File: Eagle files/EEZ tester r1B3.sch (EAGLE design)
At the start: 89 parts, among them IC2 LM5574MTX/NOPB, K1 RT314005, Q1 2N7002, Q2 2N7002, Q3 2N7002, Q4 2N7002, Q5 2N7002, Q6 2N7002, SW1 1301.9316, SW2 1301.9316, X1 39303035, X3 SSW-113-02-S-D-RA, X4 ???, X6 09185166324

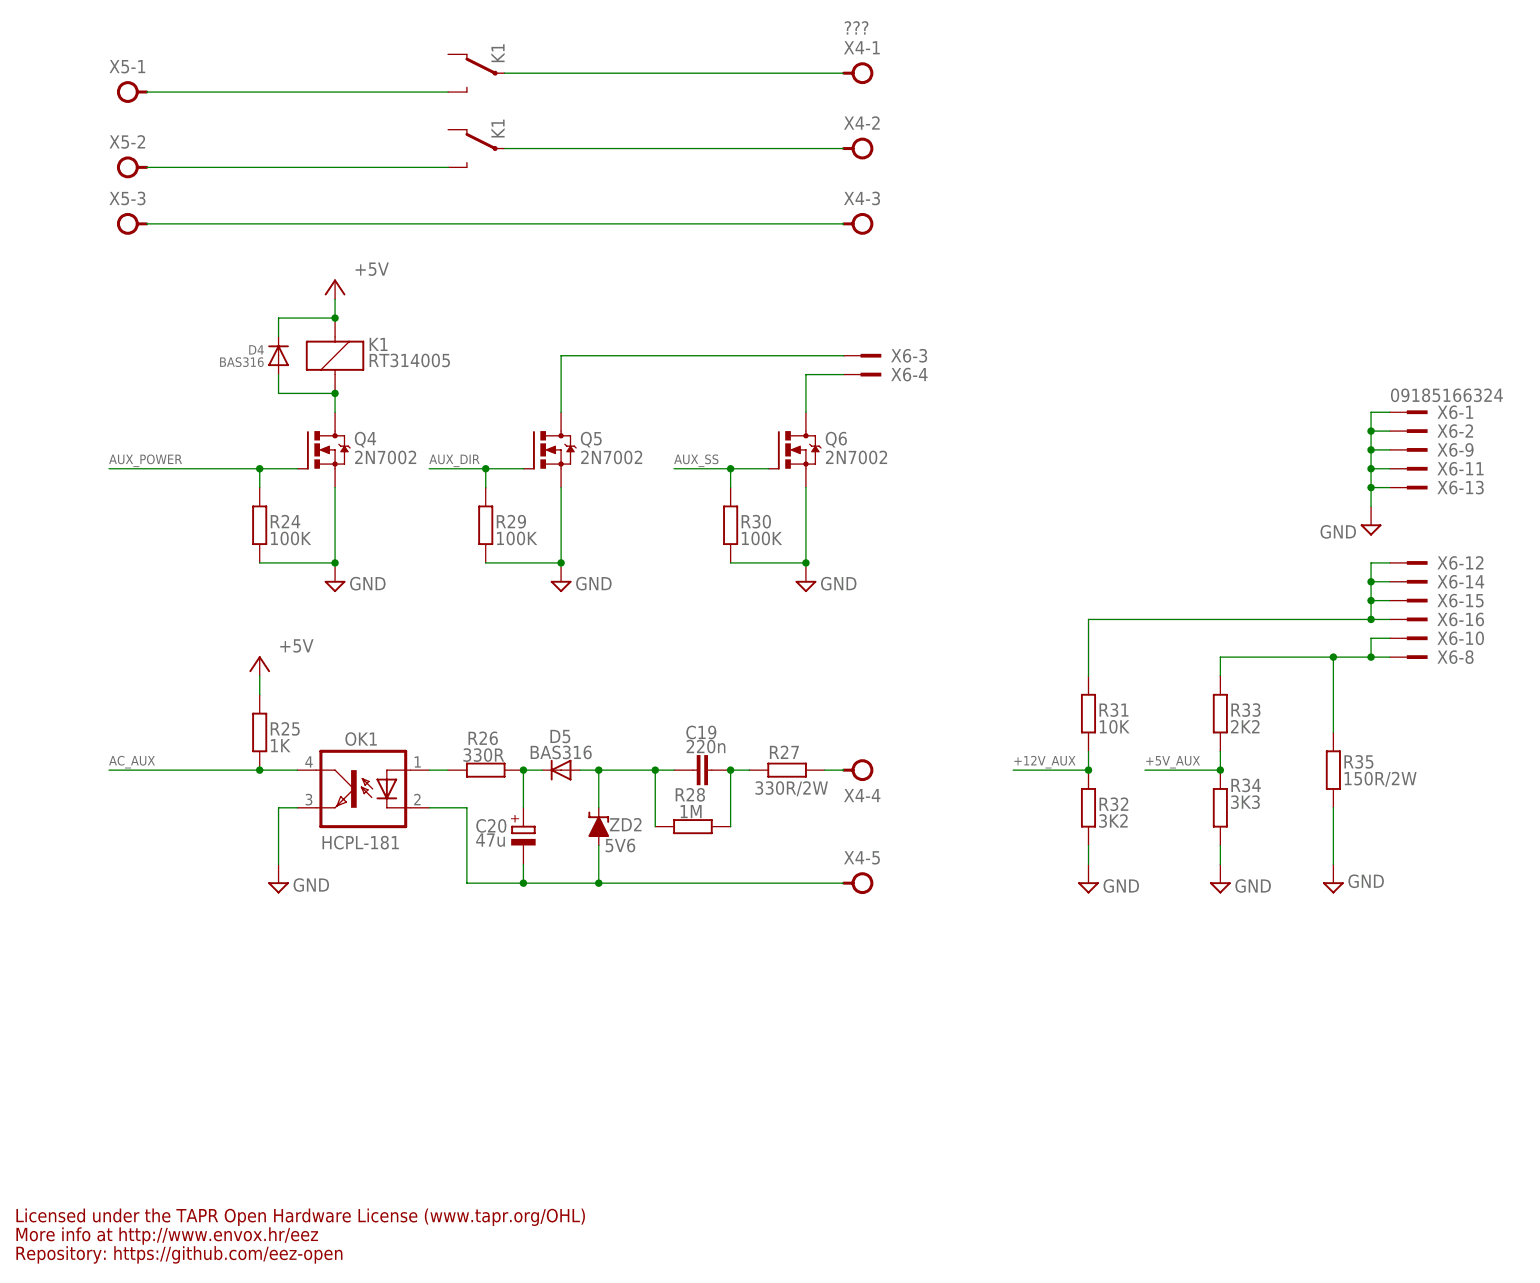
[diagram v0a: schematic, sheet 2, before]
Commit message: Arduino rotated ICSP fixed
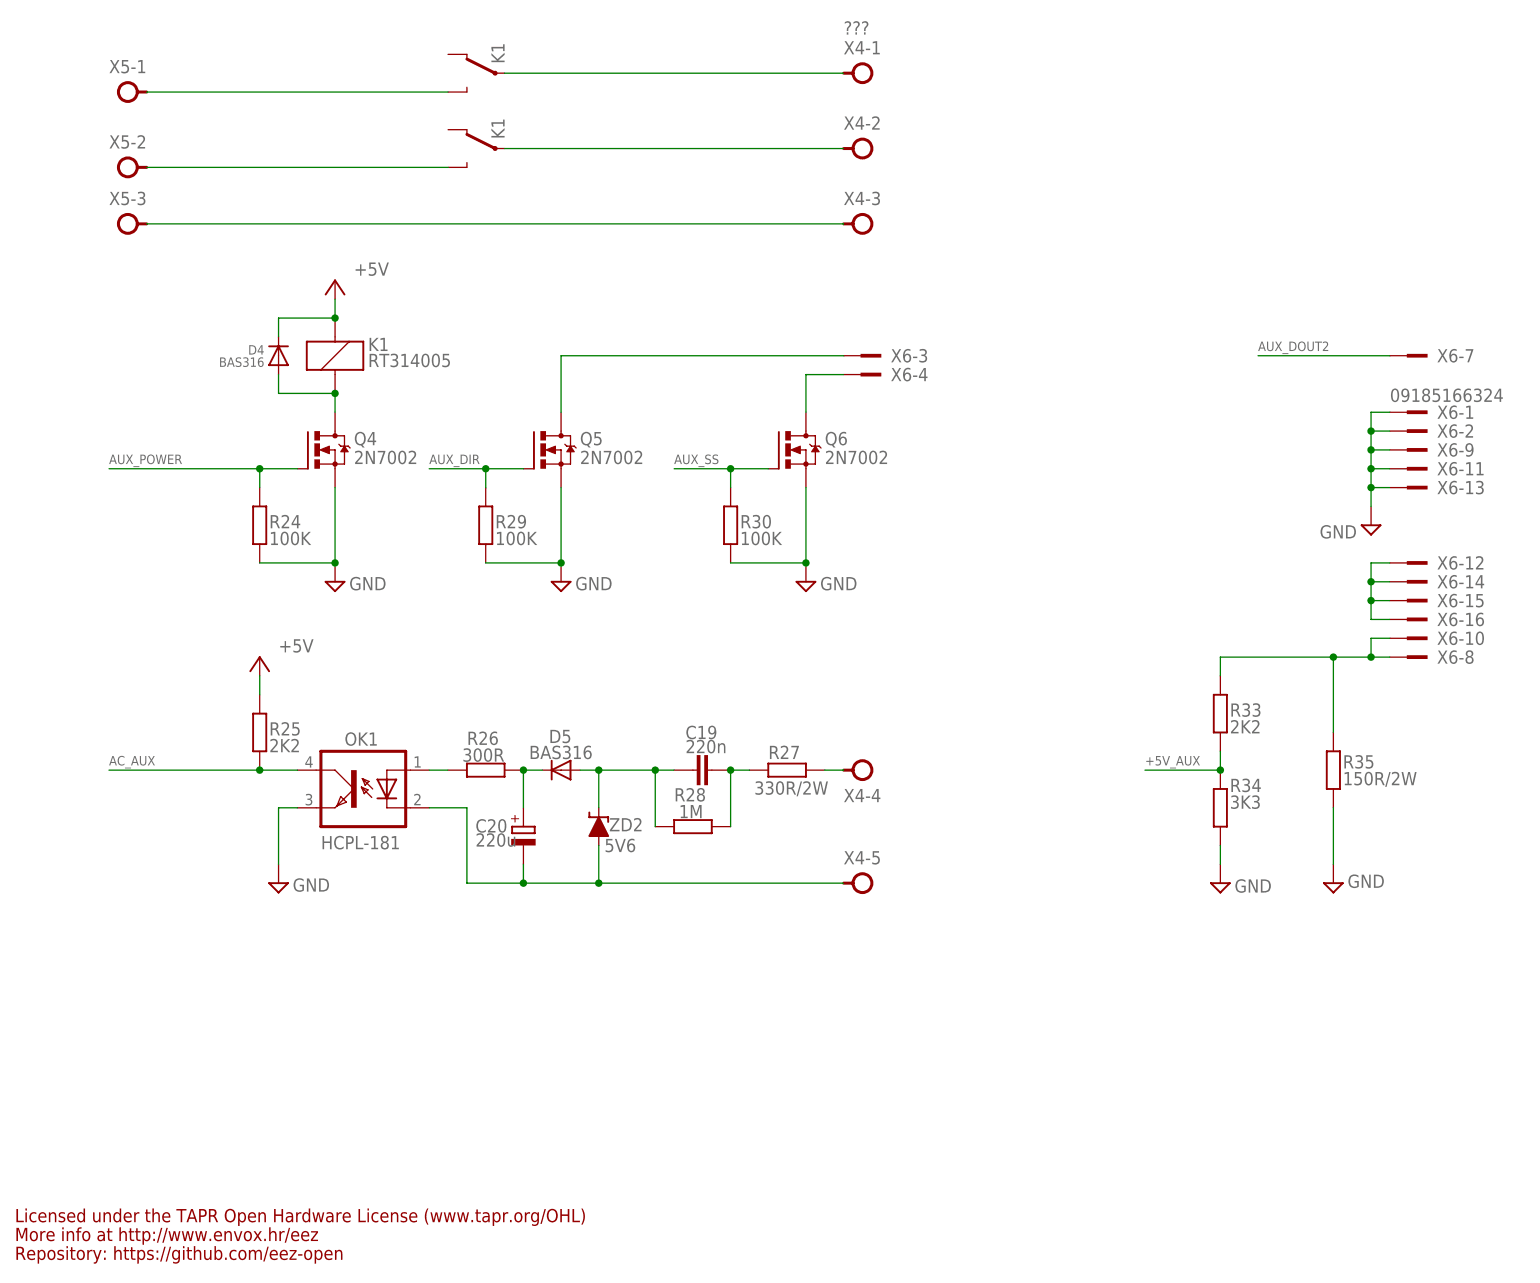
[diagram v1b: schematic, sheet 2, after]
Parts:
- removed R31: 10K, rcl:R-EU_R0805
- removed R32: 3K2, rcl:R-EU_R0805
- C17: value 4n7 -> 6n8
- C20: value 47u -> 220u
- L2: value 100uH -> 220uH
- R17: value (none) -> 10K
- R18: value (none) -> 20K
- R21: value 30K -> 18K
- R22: value 11K -> 20K
- R25: value 1K -> 2K2
- R26: value 330R -> 300R
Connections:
- net N$12 renamed LED_GREEN
- net N$14 renamed LED_RED
- net N$17 renamed SW2
- net N$18 renamed DC_ENABLE
- net N$6 renamed RPROG
- net N$8 renamed LOAD_ENABLE
- removed net +12V_AUX: MCU-ANALOG.ADC0, R31.1, R32.2
- new net AUX_DOUT2: MCU-ANALOG.ADC0, X6-7.1
- net GND: no longer R32.1
- net N$38: no longer R31.2
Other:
- note added: "Dout2 (Output) 7"
- note removed: "Sync (Output) 7"

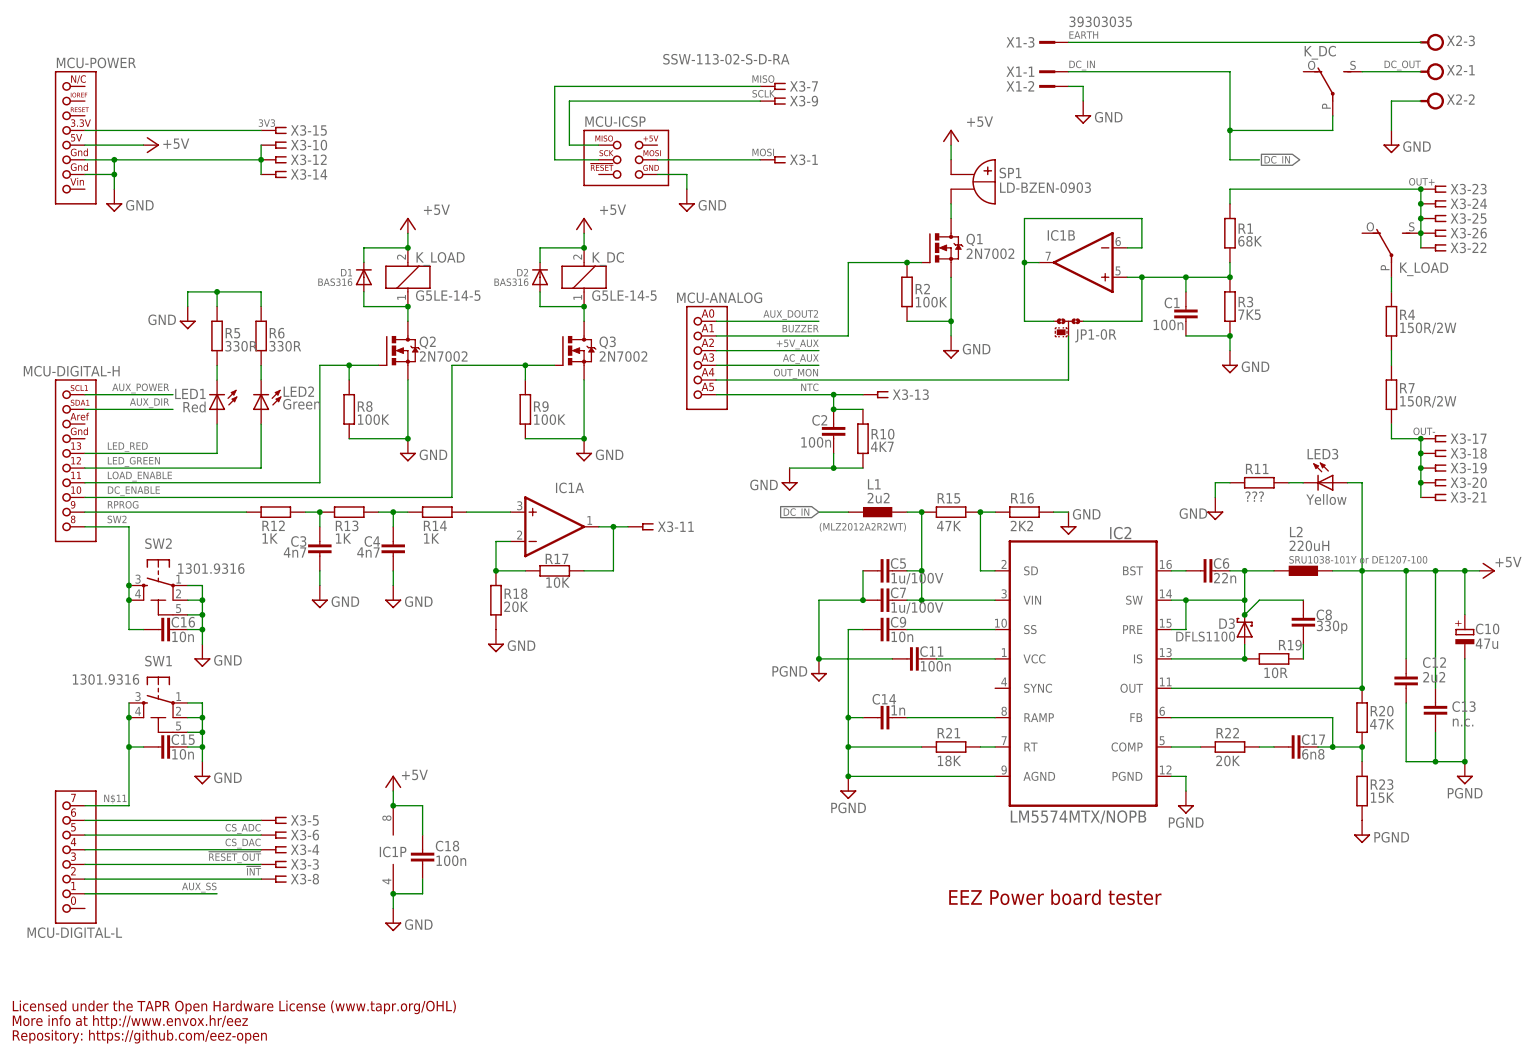
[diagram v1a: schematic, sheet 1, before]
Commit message: parts value corrections
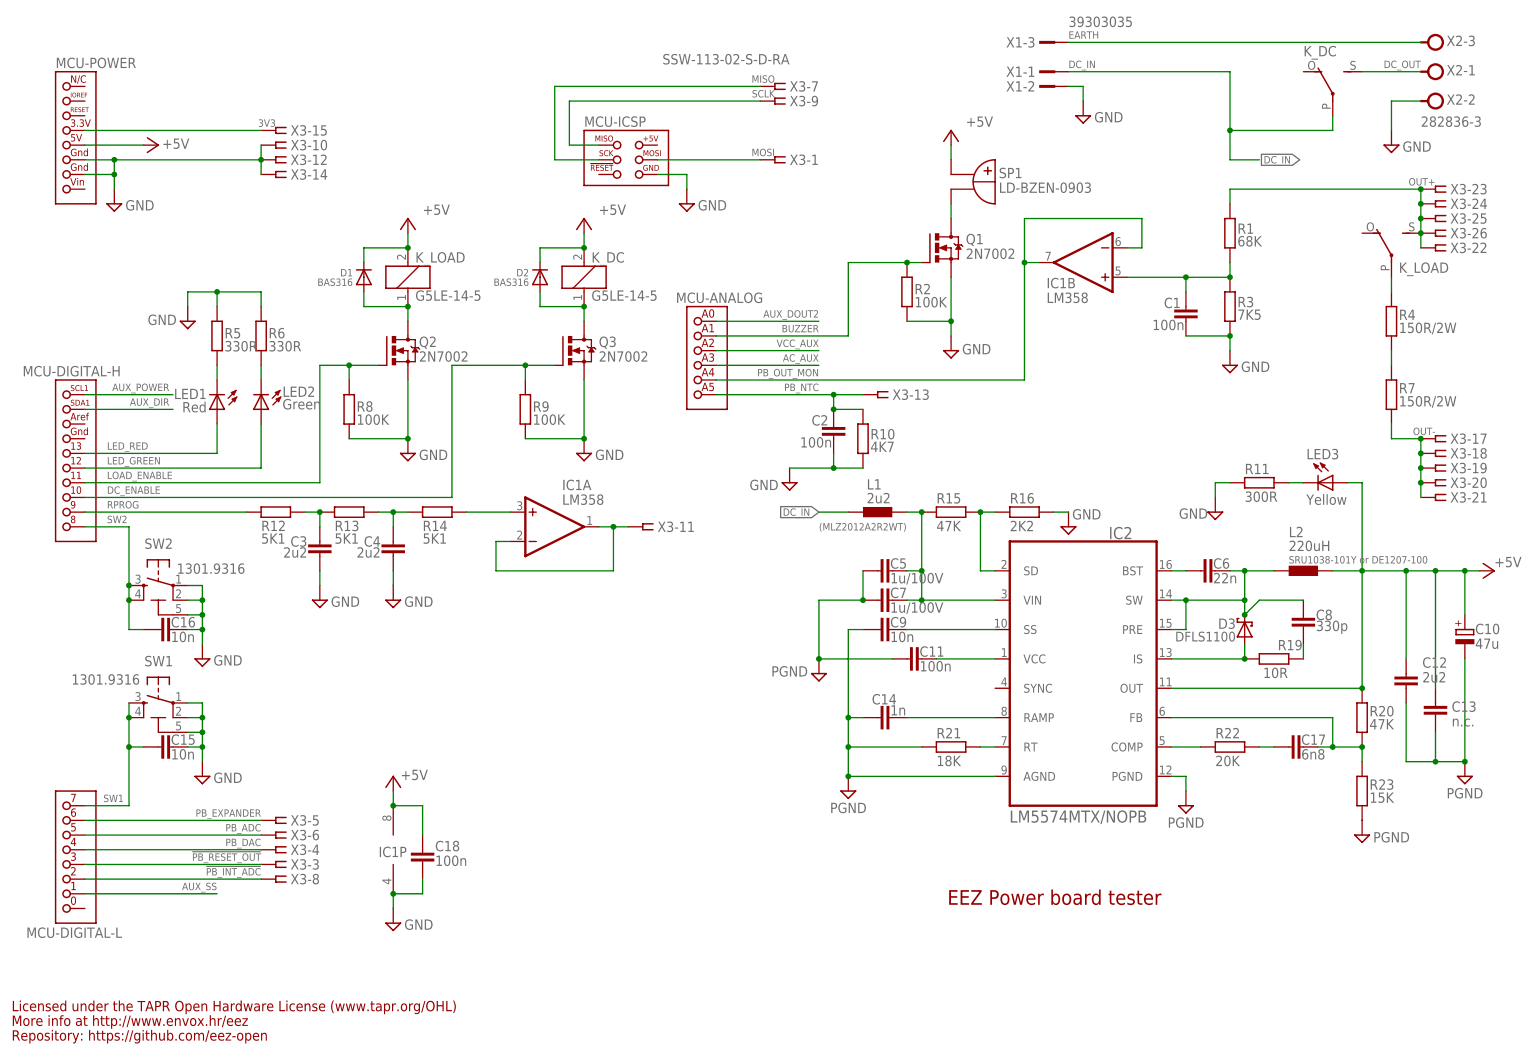
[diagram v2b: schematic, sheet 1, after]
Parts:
- removed JP1: 0R-JUMPA, jump-0r-smd:0R-JUMPA
- removed R17: 10K, rcl:R-EU_R0805
- removed R18: 20K, rcl:R-EU_R0805
- C3, C4: value 4n7 -> 2u2
- IC1: value (none) -> LM358
- R11: value ??? -> 300R
- R12, R13, R14: value 1K -> 5K1
- X2, X5: value (none) -> 282836-3
- X4: value ??? -> 282836-5
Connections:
- net !INT renamed !PB_INT_ADC
- net !RESET_OUT renamed !PB_RESET_OUT
- net +5V_AUX renamed VCC_AUX
- net CS_ADC renamed PB_ADC
- net CS_DAC renamed PB_DAC
- net CS_EXPANDER renamed PB_EXPANDER
- net NTC renamed PB_NTC
- removed net N$11: C15.1, MCU-DIGITAL-L.7(PH4), SW1.3, SW1.4
- removed net N$223: IC1A.-IN, R17.1, R18.1
- removed net N$5: IC1B.-IN, IC1B.OUT, JP1-0R.3
- removed net OUT_MON: JP1-0R.2, MCU-ANALOG.ADC4
- new net PB_OUT_MON: IC1B.-IN, IC1B.OUT, MCU-ANALOG.ADC4
- new net SW: C6.1, C8.1, D3.C, IC2.PRE, IC2.SW, L2.1
- net AUX_USET: now also IC1A.-IN; no longer R17.2
- net GND: no longer R18.2
- net N$7: no longer JP1-0R.1
- net SW1: now also C15.1, MCU-DIGITAL-L.7(PH4), SW1.3, SW1.4; no longer C6.1, C8.1, D3.C, IC2.PRE, IC2.SW, L2.1
